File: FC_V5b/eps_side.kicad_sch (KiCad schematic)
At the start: 69 parts, among them IC6 LT3652IMSE#PBF, J10 INHIBIT_P2, J11 DF11CZ-12DP-2V(27), J13 Bypass, J14 Battery Input, J17 Face4 (Z- Face), J19 ISS_INHIBIT, J2 DF11CZ-12DP-2V(27), J20 RBF_Inhibit, J21 Heater Output, J29 INHIBIT_S2, J7 INHIBIT_P1, J8 INHIBIT_S1, U10 TPS54226PWPRPWP14_2P31X2P46-L, U13 TPS7A4501DCQT, U14 INA219AxD, U15 INA219AxD, U17 LMC555CMX/NOPB, U20 74LVC1G04, U9 MCP23017_SS

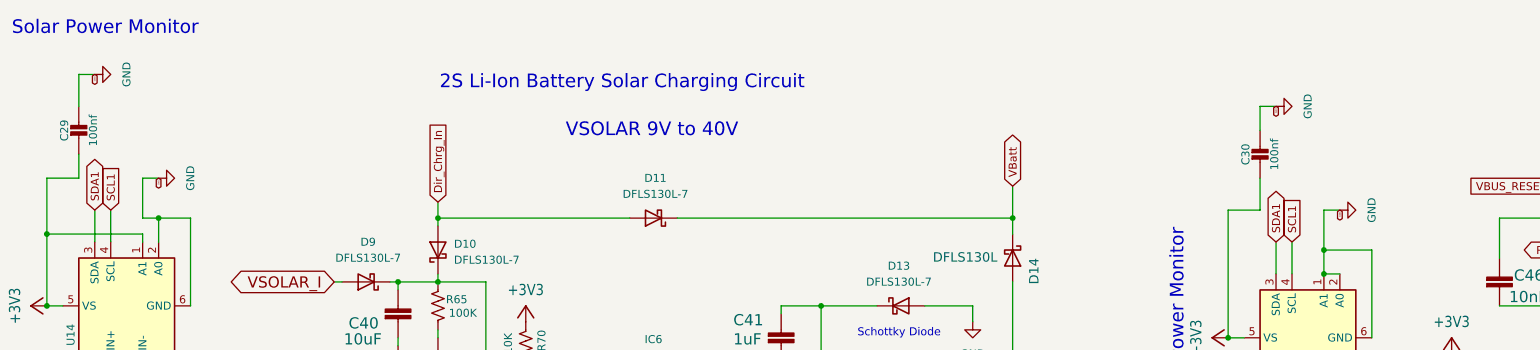
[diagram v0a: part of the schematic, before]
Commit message: Updated References with I2C Addresses
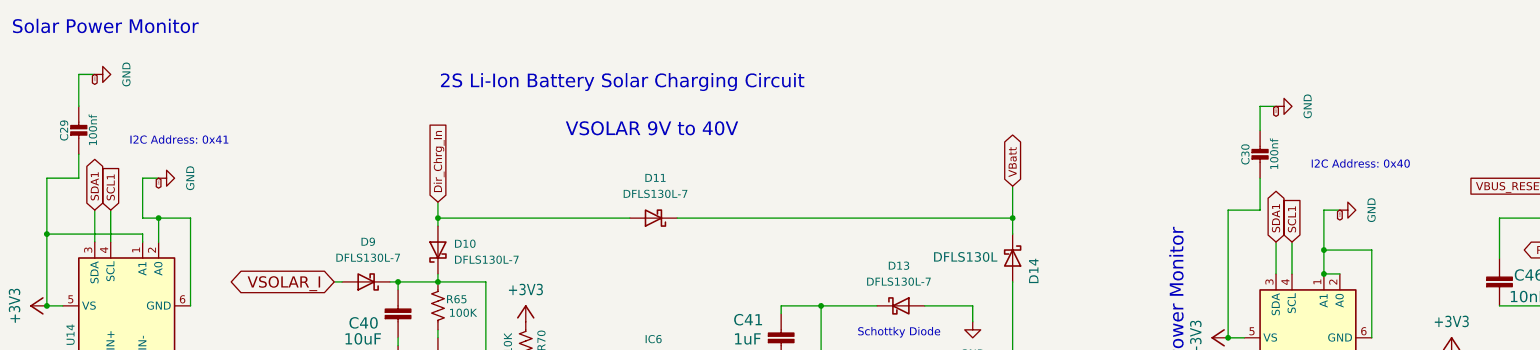
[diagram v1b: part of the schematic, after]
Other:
- note added: "I2C Address: 0x40"
- note added: "I2C Address: 0x41"
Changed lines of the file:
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@@
 	(generator_version "9.0")
 	(paper "A3")
+	(text "I2C Address: 0x41"
+		(exclude_from_sim no)
+		(at 40.132 25.908 0)
+		(effects
+			(font
+				(size 1.27 1.27)
+			)
+		)
+	)
 	(text "Regulator - 3.3V OUT"
 		(exclude_from_sim no)
@@
 		)
 	)
+	(text "I2C Address: 0x40"
+		(exclude_from_sim no)
+		(at 228.092 29.718 0)
+		(effects
+			(font
+				(size 1.27 1.27)
+			)
+		)
+	)
 	(text "555 Timer creats a pulse for \nOne Shot Regulator Reset"
 		(exclude_from_sim no)
@@
 		)
 		(instances
-			(project "FC_V5a_Rev1"
+			(project "FC_V5b"
 				(path "/c64c0d72-a9f6-4f3a-891e-1f647558f538/7cbc73fc-c188-4597-842f-d15f69db7471"
 					(page "5")

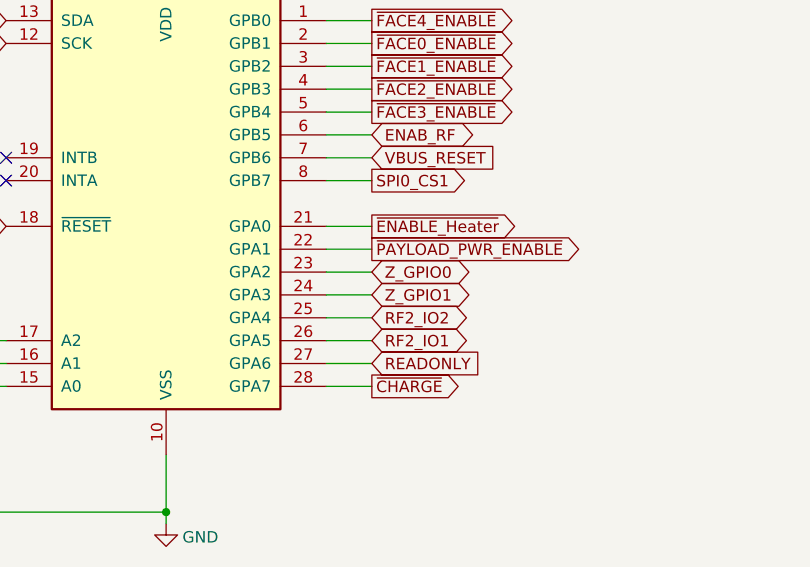
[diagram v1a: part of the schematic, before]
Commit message: Removed Z- GPIO
Also making Progress on Load Switch Update
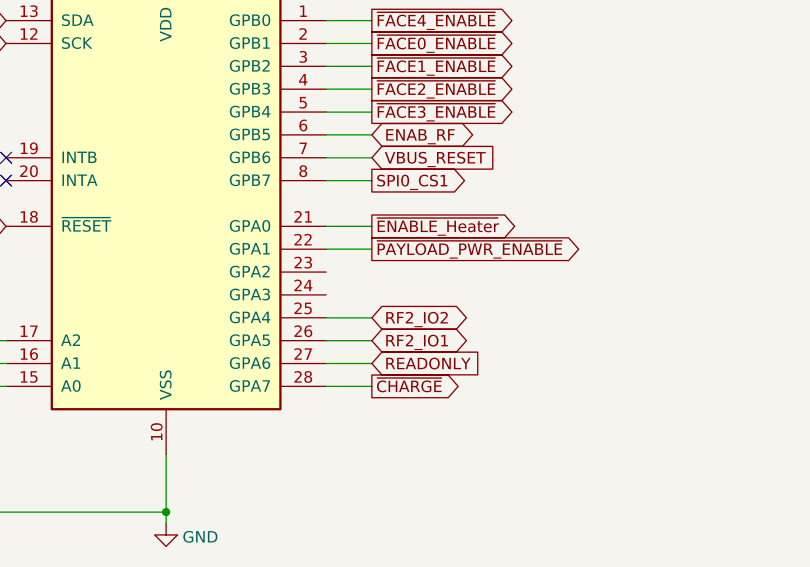
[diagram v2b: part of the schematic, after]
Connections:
- net Z_GPIO0: no longer U9.23 (GPA2)
- net Z_GPIO1: no longer U9.24 (GPA3)
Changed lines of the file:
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@@
 	(wire
 		(pts
-			(xy 92.71 189.23) (xy 97.79 189.23)
-		)
-		(stroke
-			(width 0)
-			(type default)
-		)
-	)
-	(wire
-		(pts
 			(xy 144.78 269.24) (xy 144.78 271.78)
 		)
@@
 	(wire
 		(pts
-			(xy 92.71 186.69) (xy 97.79 186.69)
-		)
-		(stroke
-			(width 0)
-			(type default)
-		)
-	)
-	(wire
-		(pts
 			(xy 345.44 68.58) (xy 345.44 71.12)
 		)
@@
 		)
 	)
-	(global_label "Z_GPIO0"
-		(shape bidirectional)
-		(at 97.79 186.69 0)
-		(fields_autoplaced yes)
-		(effects
-			(font
-				(size 1.27 1.27)
-			)
-			(justify left)
-		)
-		(property "Intersheetrefs" "${INTERSHEET_REFS}"
-			(at 109.7484 186.69 0)
-			(effects
-				(font
-					(size 1.27 1.27)
-				)
-				(justify left)
-				(hide yes)
-			)
-		)
-	)
 	(global_label "F2_SDA"
 		(shape output)
@@
 			(effects
 				(font
-					(size 1.27 1.27)
-				)
-				(justify left)
-				(hide yes)
-			)
-		)
-	)
-	(global_label "Z_GPIO1"
-		(shape bidirectional)
-		(at 97.79 189.23 0)
-		(fields_autoplaced yes)
-		(effects
-			(font
-				(size 1.27 1.27)
-			)
-			(justify left)
-		)
-		(property "Intersheetrefs" "${INTERSHEET_REFS}"
-			(at 109.7484 189.23 0)
-			(effects
-				(font

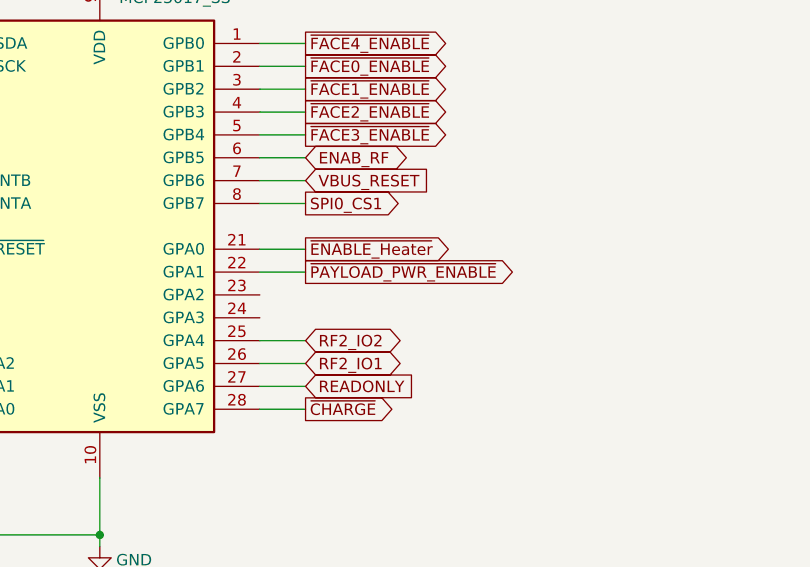
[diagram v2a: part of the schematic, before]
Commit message: Added TPS2 and TPS4 Load Switch Schematics
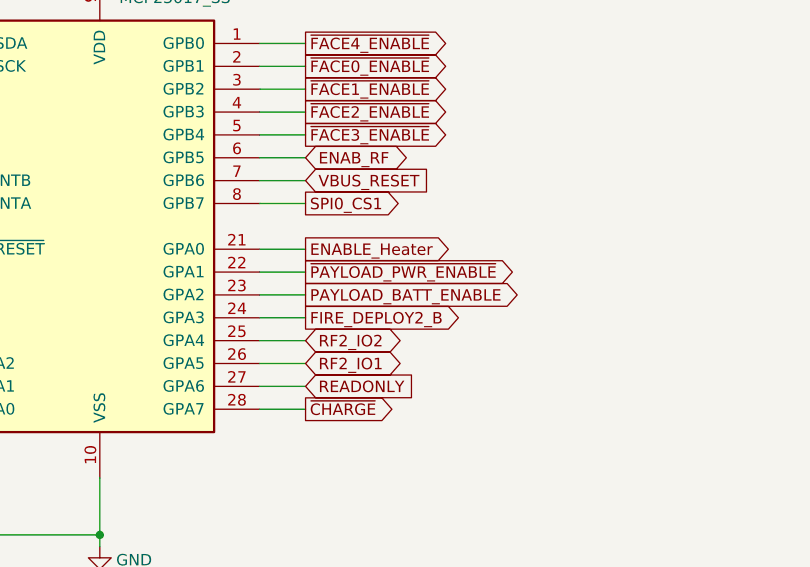
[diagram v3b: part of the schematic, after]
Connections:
- net PAYLOAD_BATT_ENABLE: now reaches U9.23 (GPA2)
- net FIRE_DEPLOY2_B: now reaches U9.24 (GPA3)
- net ~{ENABLE_Heater} renamed ENABLE_Heater
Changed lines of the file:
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@@
+	(wire
+		(pts
+			(xy 92.71 189.23) (xy 97.79 189.23)
+		)
+		(stroke
+			(width 0)
+			(type default)
+		)
+	)
 	(wire
 		(pts
@@
 		(pts
 			(xy 119.38 38.1) (xy 172.72 38.1)
+		)
+		(stroke
+			(width 0)
+			(type default)
+		)
+	)
+	(wire
+		(pts
+			(xy 92.71 186.69) (xy 97.79 186.69)
 		)
 		(stroke
@@
 		)
 	)
-	(global_label "~{ENABLE_Heater}"
+	(global_label "ENABLE_Heater"
 		(shape output)
 		(at 97.79 181.61 0)
@@
 		)
 	)
+	(global_label "FIRE_DEPLOY2_B"
+		(shape output)
+		(at 97.79 189.23 0)
+		(fields_autoplaced yes)
+		(effects
+			(font
+				(size 1.27 1.27)
+			)
+			(justify left)
+		)
+		(property "Intersheetrefs" "${INTERSHEET_REFS}"
+			(at 116.4385 189.23 0)
+			(effects
+				(font
+					(size 1.27 1.27)
+				)
+				(justify left)
+				(hide yes)
+			)
+		)
+	)
 	(global_label "RF2_IO2"
 		(shape bidirectional)
@@
 			(effects
 				(font
+					(size 1.27 1.27)
+				)
+				(justify left)
+				(hide yes)
+			)
+		)
+	)
+	(global_label "PAYLOAD_BATT_ENABLE"
+		(shape output)
+		(at 97.79 186.69 0)
+		(fields_autoplaced yes)
+		(effects
+			(font
+				(size 1.27 1.27)
+			)
+			(justify left)
+		)
+		(property "Intersheetrefs" "${INTERSHEET_REFS}"
+			(at 122.1838 186.69 0)
+			(effects
+				(font

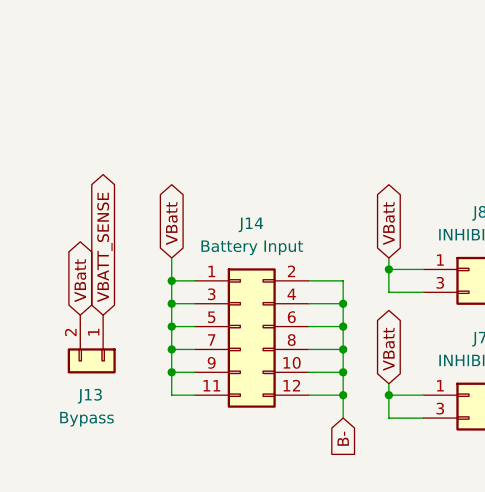
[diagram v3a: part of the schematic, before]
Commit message: Removed Inhibit Bypass Jumper
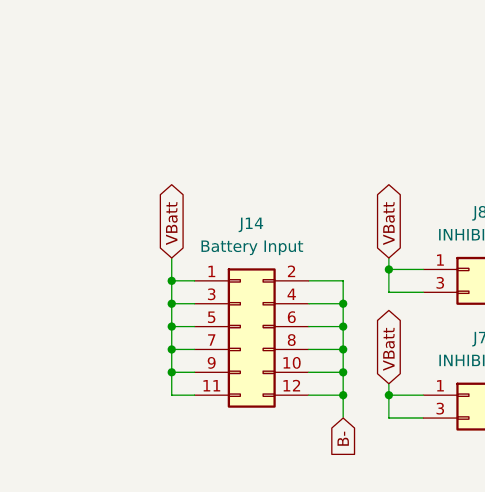
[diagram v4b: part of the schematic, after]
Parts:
- removed J13: Bypass, Connector_PinSocket_2.54mm:PinSocket_1x02_P2.54mm_Vertical, symbol Connector_Generic:Conn_01x02
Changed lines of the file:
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@@
 		)
 	)
-	(global_label "VBATT_SENSE"
-		(shape bidirectional)
-		(at 21.59 267.97 90)
-		(fields_autoplaced yes)
-		(effects
-			(font
-				(size 1.27 1.27)
-			)
-			(justify left)
-		)
-		(property "Intersheetrefs" "${INTERSHEET_REFS}"
-			(at 21.5106 253.1593 90)
-			(effects
-				(font
-					(size 1.27 1.27)
-				)
-				(justify left)
-				(hide yes)
-			)
-		)
-	)
 	(global_label "VSOLAR"
 		(shape bidirectional)
@@
 		)
 	)
-	(global_label "VBatt"
-		(shape bidirectional)
-		(at 19.05 267.97 90)
-		(fields_autoplaced yes)
-		(effects
-			(font
-				(size 1.27 1.27)
-			)
-			(justify left)
-		)
-		(property "Intersheetrefs" "${INTERSHEET_REFS}"
-			(at 18.9706 260.5979 90)
-			(effects
-				(font
-					(size 1.27 1.27)
-				)
-				(justify left)
-				(hide yes)
-			)
-		)
-	)
 	(global_label "F0_PWR"
 		(shape output)
@@
 					(unit 1)
 				)
-			)
-		)
-	)
-	(symbol
-		(lib_id "Connector_Generic:Conn_01x02")
-		(at 21.59 273.05 270)
-		(unit 1)
-		(exclude_from_sim no)
-		(in_bom yes)
-		(on_board yes)
-		(dnp no)
-		(property "Reference" "J13"
-			(at 21.59 276.86 90)
-			(effects
-				(font
-					(size 1.27 1.27)
-				)
-				(justify right)
-			)
-		)
-		(property "Value" "Bypass"
-			(at 22.86 279.4 90)
-			(effects
-				(font
-					(size 1.27 1.27)
-				)
-				(justify right)
-			)
-		)
-		(property "Footprint" "Connector_PinSocket_2.54mm:PinSocket_1x02_P2.54mm_Vertical"
-			(at 21.59 273.05 0)
-			(effects
-				(font
-					(size 1.27 1.27)
-				)
-				(hide yes)
-			)
-		)
-		(property "Datasheet" "~"
-			(at 21.59 273.05 0)
-			(effects
-				(font
-					(size 1.27 1.27)
-				)
-				(hide yes)
-			)
-		)
-		(property "Description" ""
-			(at 21.59 273.05 0)
-			(effects
-				(font
-					(size 1.27 1.27)
-				)
-				(hide yes)
-			)
-		)
-		(pin "1"
-		)
-		(pin "2"
-		)
-		(instances
-			(project "FC_V5"
-				(path "/c64c0d72-a9f6-4f3a-891e-1f647558f538/7cbc73fc-c188-4597-842f-d15f69db7471"
-					(reference "J13")
-					(unit 1)
-				)

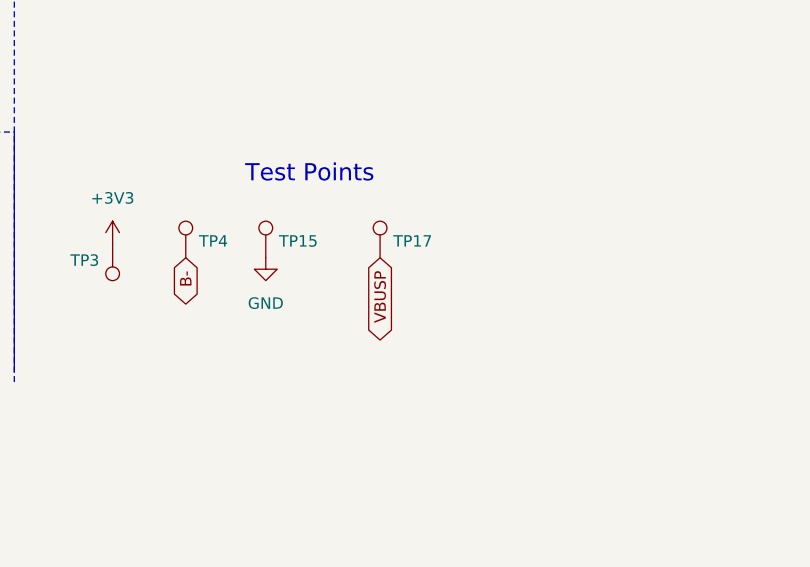
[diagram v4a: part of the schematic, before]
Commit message: Repositioned Sys INA and Removed VBUSP TP
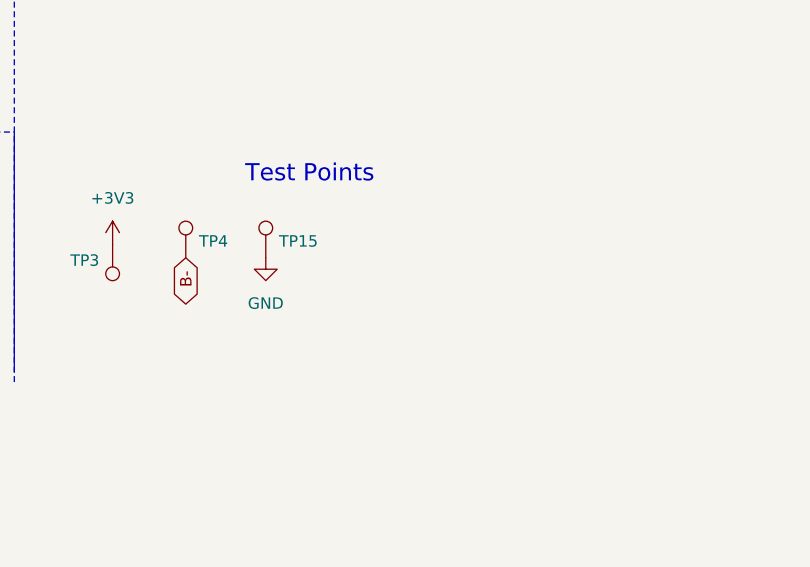
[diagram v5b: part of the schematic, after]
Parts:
- removed TP17: TestPoint, TestPoint:TestPoint_Loop_D1.80mm_Drill1.0mm_Beaded, symbol Connector:TestPoint
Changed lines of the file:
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@@
 		)
 	)
-	(global_label "VBUSP"
-		(shape bidirectional)
-		(at 340.36 240.03 270)
-		(fields_autoplaced yes)
-		(effects
-			(font
-				(size 1.27 1.27)
-			)
-			(justify right)
-		)
-		(property "Intersheetrefs" "${INTERSHEET_REFS}"
-			(at 340.2806 248.6117 90)
-			(effects
-				(font
-					(size 1.27 1.27)
-				)
-				(justify right)
-				(hide yes)
-			)
-		)
-	)
 	(global_label "~{FACE2_ENABLE}"
 		(shape output)
@@
 			)
 		)
-		(property "Datasheet" "~"
+		(property "Datasheet" "https://www.diodes.com/assets/Datasheets/DFLS130L.pdf"
 			(at 172.72 44.45 0)
 			(effects
@@
 			)
 		)
-		(property "Datasheet" "~"
+		(property "Datasheet" "https://www.diodes.com/assets/Datasheets/DFLS130L.pdf"
 			(at 115.57 38.1 0)
 			(effects
@@
 			)
 		)
-		(property "Datasheet" "~"
+		(property "Datasheet" "https://www.diodes.com/assets/Datasheets/DFLS130L.pdf"
 			(at 81.28 43.18 0)
 			(effects
@@
 					(unit 1)
 				)
-			)
-		)
-	)
-	(symbol
-		(lib_id "Connector:TestPoint")
-		(at 340.36 240.03 0)
-		(unit 1)
-		(exclude_from_sim no)
-		(in_bom yes)
-		(on_board yes)
-		(dnp no)
-		(property "Reference" "TP17"
-			(at 341.8332 238.2012 0)
-			(effects
-				(font
-					(size 1.27 1.27)
-				)
-				(justify left)
-			)
-		)
-		(property "Value" "TestPoint"
-			(at 341.8332 239.3442 0)
-			(effects
-				(font
-					(size 1.27 1.27)
-				)
-				(justify left)
-				(hide yes)
-			)
-		)
-		(property "Footprint" "TestPoint:TestPoint_Loop_D1.80mm_Drill1.0mm_Beaded"
-			(at 345.44 240.03 0)
-			(effects
-				(font
-					(size 1.27 1.27)
-				)
-				(hide yes)
-			)
-		)
-		(property "Datasheet" "~"
-			(at 345.44 240.03 0)
-			(effects
-				(font
-					(size 1.27 1.27)
-				)
-				(hide yes)
-			)
-		)
-		(property "Description" ""
-			(at 340.36 240.03 0)
-			(effects
-				(font
-					(size 1.27 1.27)
-				)
-				(hide yes)
-			)
-		)
-		(pin "1"
-		)
-		(instances
-			(project "FC_V5"
-				(path "/c64c0d72-a9f6-4f3a-891e-1f647558f538/7cbc73fc-c188-4597-842f-d15f69db7471"
-					(reference "TP17")
-					(unit 1)
-				)

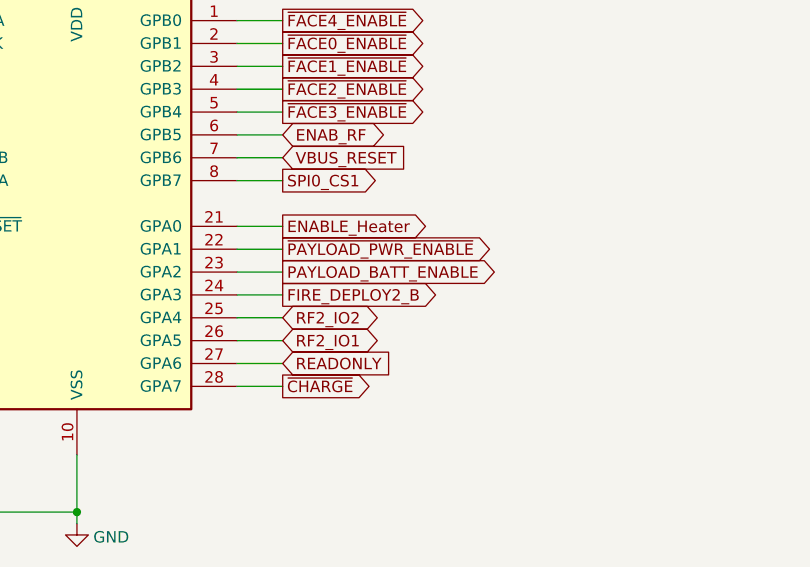
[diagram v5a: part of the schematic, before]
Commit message: Completed Layout of New TSP2 and TPS4 Load Switches
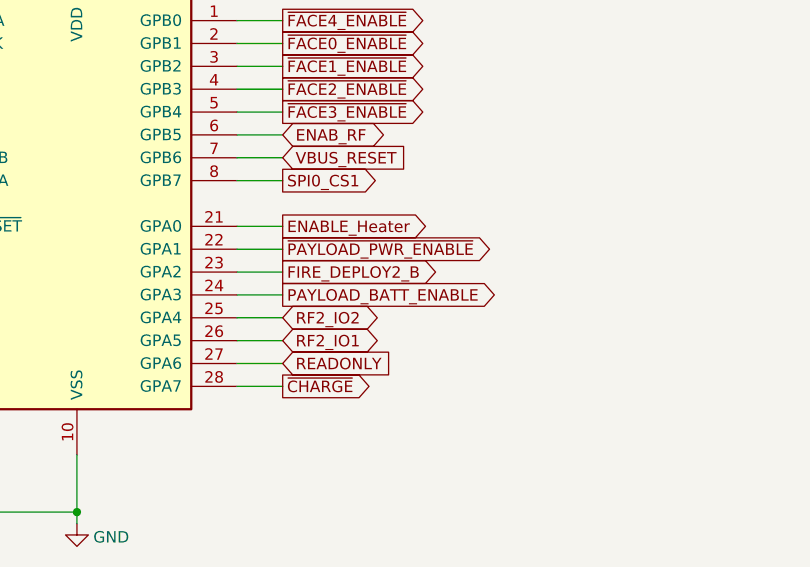
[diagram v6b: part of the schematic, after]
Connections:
- net FIRE_DEPLOY2_B: now also U9.23 (GPA2); no longer U9.24 (GPA3)
- net PAYLOAD_BATT_ENABLE: now also U9.24 (GPA3); no longer U9.23 (GPA2)
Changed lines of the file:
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@@
+		)
+	)
+	(global_label "PAYLOAD_BATT_ENABLE"
+		(shape output)
+		(at 97.79 189.23 0)
+		(fields_autoplaced yes)
+		(effects
+			(font
+				(size 1.27 1.27)
+			)
+			(justify left)
+		)
+		(property "Intersheetrefs" "${INTERSHEET_REFS}"
+			(at 122.1838 189.23 0)
+			(effects
+				(font
+					(size 1.27 1.27)
+				)
+				(justify left)
+				(hide yes)
+			)
 		)
 	)
@@
 	(global_label "FIRE_DEPLOY2_B"
 		(shape output)
-		(at 97.79 189.23 0)
-		(fields_autoplaced yes)
-		(effects
-			(font
-				(size 1.27 1.27)
-			)
-			(justify left)
-		)
-		(property "Intersheetrefs" "${INTERSHEET_REFS}"
-			(at 116.4385 189.23 0)
+		(at 97.79 186.69 0)
+		(fields_autoplaced yes)
+		(effects
+			(font
+				(size 1.27 1.27)
+			)
+			(justify left)
+		)
+		(property "Intersheetrefs" "${INTERSHEET_REFS}"
+			(at 116.4385 186.69 0)
 			(effects
 				(font
@@
 			(effects
 				(font
-					(size 1.27 1.27)
-				)
-				(justify left)
-				(hide yes)
-			)
-		)
-	)
-	(global_label "PAYLOAD_BATT_ENABLE"
-		(shape output)
-		(at 97.79 186.69 0)
-		(fields_autoplaced yes)
-		(effects
-			(font
-				(size 1.27 1.27)
-			)
-			(justify left)
-		)
-		(property "Intersheetrefs" "${INTERSHEET_REFS}"
-			(at 122.1838 186.69 0)
-			(effects
-				(font
